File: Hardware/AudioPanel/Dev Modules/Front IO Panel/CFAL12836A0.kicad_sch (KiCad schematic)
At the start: 3 parts, among them U35 CFAL12836A0-088

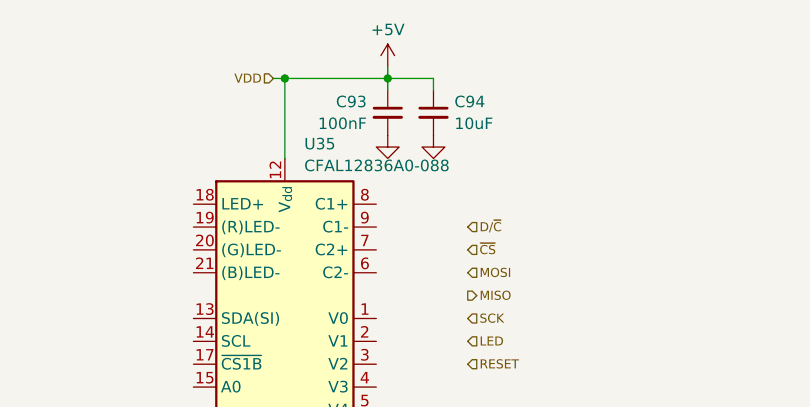
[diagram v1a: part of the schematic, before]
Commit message: Added level shifters for all SAMD21s
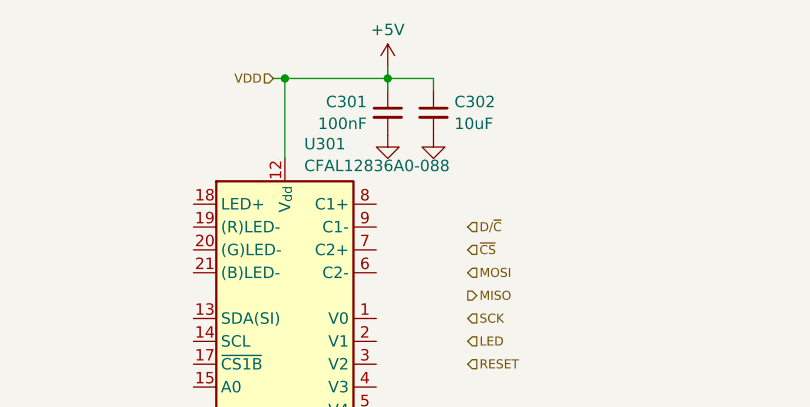
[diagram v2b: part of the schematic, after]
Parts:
- renumbered C93 to C301, C94 to C302, U35 to U301
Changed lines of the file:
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@@
 		(dnp no)
 		(fields_autoplaced yes)
-		(property "Reference" "#PWR?"
+		(property "Reference" "#PWR0301"
 			(at 212.09 86.36 0)
 			(effects
@@
 			(project "Front IO Panel"
 				(path "/5115d310-a9f7-4cd2-bb07-2c33745c004f/c4aba118-8bcc-46b5-ab7c-9e20931e6787"
-					(reference "#PWR?")
+					(reference "#PWR0301")
 					(unit 1)
 				)
@@
 		(dnp no)
 		(fields_autoplaced yes)
-		(property "Reference" "#PWR?"
+		(property "Reference" "#PWR0302"
 			(at 212.09 96.52 0)
 			(effects
@@
 			(project "Front IO Panel"
 				(path "/5115d310-a9f7-4cd2-bb07-2c33745c004f/c4aba118-8bcc-46b5-ab7c-9e20931e6787"
-					(reference "#PWR?")
+					(reference "#PWR0302")
 					(unit 1)
 				)
@@
 		(dnp no)
 		(fields_autoplaced yes)
-		(property "Reference" "U?"
+		(property "Reference" "U301"
 			(at 202.8033 91.1055 0)
 			(effects
@@
 			(project "Front IO Panel"
 				(path "/5115d310-a9f7-4cd2-bb07-2c33745c004f/c4aba118-8bcc-46b5-ab7c-9e20931e6787"
-					(reference "U?")
+					(reference "U301")
 					(unit 1)
 				)
@@
 		(on_board yes)
 		(dnp no)
-		(property "Reference" "C?"
+		(property "Reference" "C302"
 			(at 219.4941 86.4241 0)
 			(effects
@@
 			(project "Front IO Panel"
 				(path "/5115d310-a9f7-4cd2-bb07-2c33745c004f/c4aba118-8bcc-46b5-ab7c-9e20931e6787"
-					(reference "C?")
+					(reference "C302")
 					(unit 1)
 				)
@@
 		(on_board yes)
 		(dnp no)
-		(property "Reference" "C?"
+		(property "Reference" "C301"
 			(at 209.7659 86.4241 0)
 			(effects
@@
 			(project "Front IO Panel"
 				(path "/5115d310-a9f7-4cd2-bb07-2c33745c004f/c4aba118-8bcc-46b5-ab7c-9e20931e6787"
-					(reference "C?")
+					(reference "C301")
 					(unit 1)
 				)
@@
 		(dnp no)
 		(fields_autoplaced yes)
-		(property "Reference" "#PWR?"
+		(property "Reference" "#PWR0303"
 			(at 217.17 96.52 0)
 			(effects
@@
 			(project "Front IO Panel"
 				(path "/5115d310-a9f7-4cd2-bb07-2c33745c004f/c4aba118-8bcc-46b5-ab7c-9e20931e6787"
-					(reference "#PWR?")
-					(unit 1)
-				)
+					(reference "#PWR0303")
+					(unit 1)
+				)

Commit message: Work on front control panel
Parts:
- removed U301: CFAL12836A0-088, Display:NHD-C12832A1Z-FSRGB, symbol Display_Graphic:NHD-C12832A1Z-FSRGB
- added C303: 1u, symbol Device:C_Small
- added C304: 100u, symbol Device:C_Small_US
- added C305: 47u, symbol Device:C_Small
- added C306: 10u, symbol Device:C_Small
- added C307, C308, C309, C310, C314: 100n, symbol Device:C_Small
- added C311: 22u, symbol Device:C_Small
- added C312, C313: 4u7, symbol Device:C_Small
- added D201: Red, LED_THT:LED_D5.0mm, symbol Device:LED_Filled
- added D301: B5817WS-TP, Diode_SMD:D_SOD-323, symbol Device:D_Schottky
- added D302, D303: 1N4148X-TP, Diode_SMD:D_SOD-523, symbol Device:D
- added JP301, JP302: Jumper_2_Small_Open, Jumper:SolderJumper-2_P1.3mm_Open_Pad1.0x1.5mm, symbol Jumper:Jumper_2_Small_Open
- added L301: 10uH, 750mA, symbol Device:L
- added R201: 3k3, Libraries:Worthington_R_0603, symbol Device:R_Small_US
- added R301: 51k, symbol Device:R_Small_US
- added R302: 4k99, symbol Device:R_Small_US
- added R303: 16, symbol Device:R_Small_US
- added R304: 10k, symbol Device:R_Small_US
- added R305: 4k7, symbol Device:R_Small_US
- added TP115: TestPoint_Flag, Libraries:KEYSTONE_5017, symbol Connector:TestPoint_Flag
- added U301: CFAL12836A0, Libraries:CFAL12836A0-088, symbol Libraries:CFAL12836A0
- added U302: AP3012, Package_TO_SOT_SMD:SOT-23-5, symbol Regulator_Switching:AP3012
- C301: value 100nF -> 100n
- C302: value 10uF -> 100n
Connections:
- net GND: now also C303.2, C304.2, C305.2, C306.2, C307.2, C308.2, C309.2, C310.2, C311.2, C312.2, C313.2, C314.2, D302.1 (K), JP302.1 (A), R201.1, R302.2, R305.2, U301.1 (VSS), U301.10 (~{WR}), U301.11 (~{RD}), U301.16 (D2), U301.17 (D3), U301.18 (D4), U301.19 (D5), U301.20 (D6), U301.21 (D7), U301.22 (P/~{S}), U301.27 (VSS), U301.33 (VSS), U301.7 (VSS), U302.2 (GND)
- net MOSI: now also U301.15 (D1(SDIN))
- net SCK: now also U301.14 (D0(SCLK))
- net ~{CS}: now also U301.12 (~{CS})
- net +5V renamed +3V3
- net +3V3: now also C306.1, C309.1, C310.1, C311.1, JP301.1 (A), L301.1, U301.23 (VDDIO), U301.28 (VDD), U301.5 (VDD), U301.8 (VDDIO), U302.5 (IN)
- new net: C303.1, D301.1 (K), R301.1, R303.1
- new net: D301.2 (A), L301.2, U302.1 (SW)
- new net: C314.1, TP115.1, U301.29 (VDDL)
- new net: C312.1, C313.1, R304.1, U301.30 (VCC-R), U301.4 (VCC-R)
- new net: JP302.2 (B), R304.2, U301.6 (PSEL)
- new net: JP301.2 (B), R305.1, U302.4 (~{SHDN})
- new net: R301.2, R302.1, U302.3 (FB)
- new net: D302.2 (A), D303.1 (K)
- new net: D201.1 (K), R201.2
- new net +14V: C304.1, C305.1, C307.1, C308.1, D201.2 (A), R303.2, U301.2 (VCC-C), U301.32 (VCC-C)
- new net A0: U301.13 (A0)
- new net PRE: D303.2 (A), U301.3 (PRE), U301.31 (PRE)
- new net ~{RESET}: U301.9 (~{RST})
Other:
- note added: "3.3V to 14V Boost Supply"
- note added: "The 16ohm+ 47µF filter reduces the current ripple seen on the +3.3v supply line for certain images displayed . The power supply in the Seeeduino v4.2 produces audible noise without this filter. The noise is greatly reduced by the filter. Optionally, you can load the 100µF aluminum electrolytic capacitor which appears to eliminate the audible noise entirely."

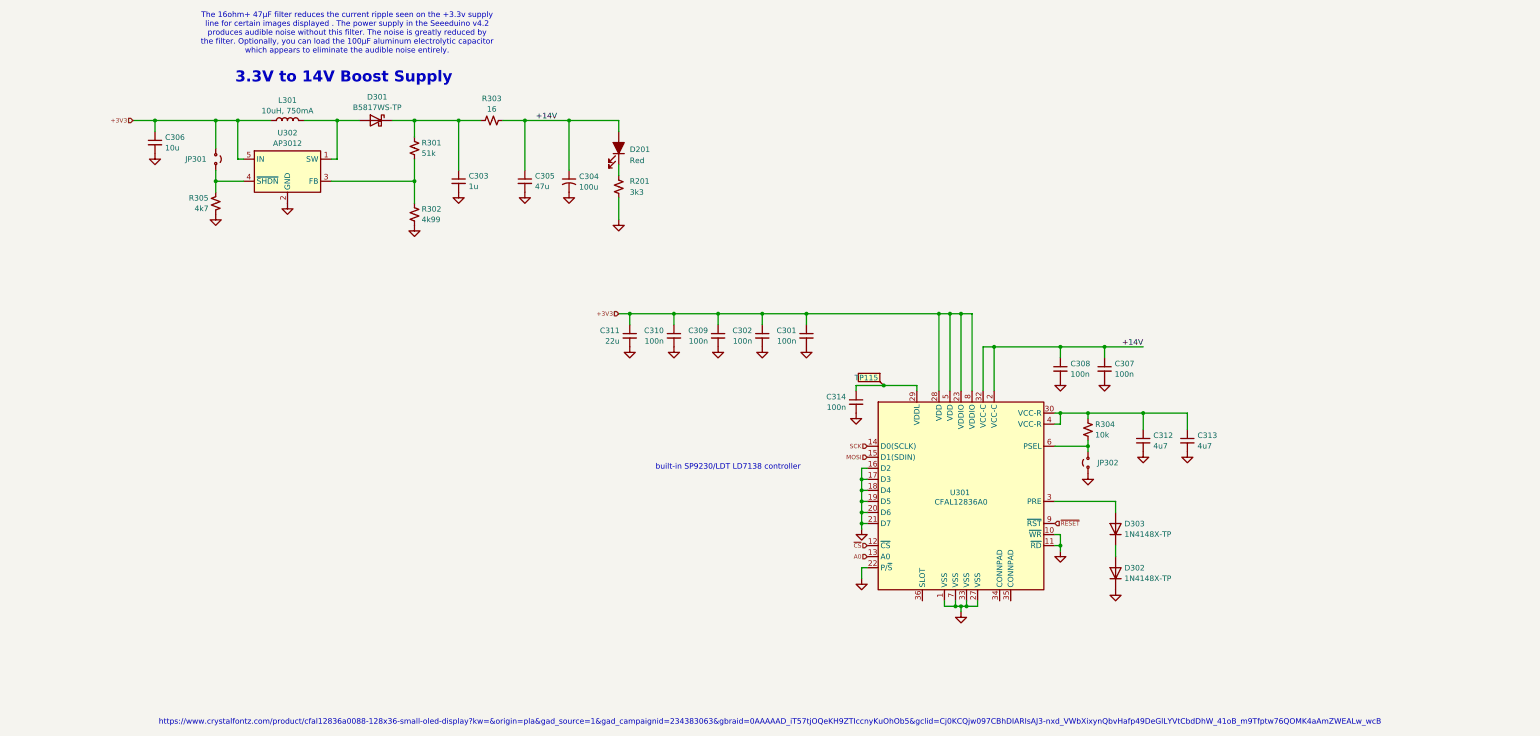
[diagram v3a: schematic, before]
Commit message: Fixed some footprints
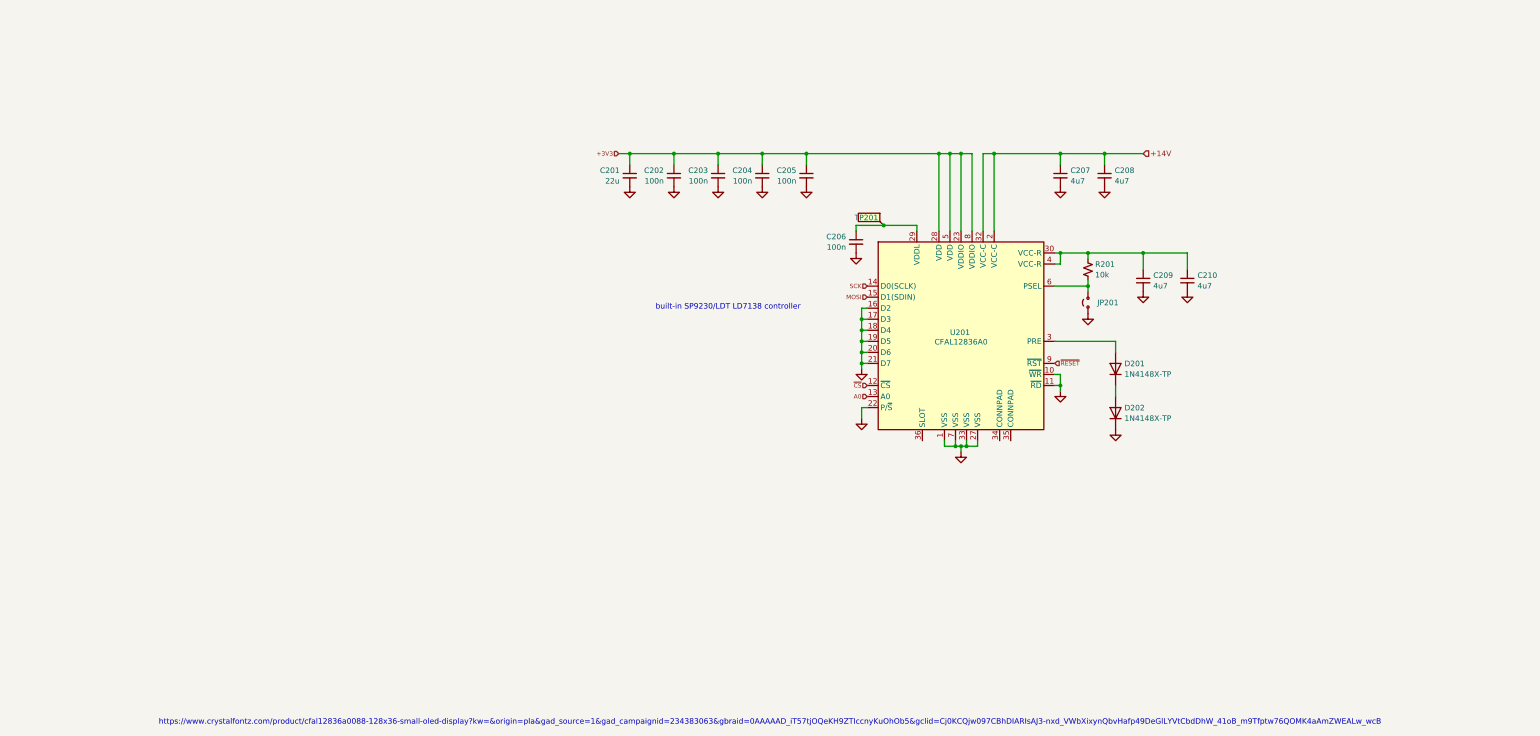
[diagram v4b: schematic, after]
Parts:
- removed C303: 1u, symbol Device:C_Small
- removed C304: 100u, symbol Device:C_Small_US
- removed C305: 47u, symbol Device:C_Small
- removed C306: 10u, symbol Device:C_Small
- removed C307, C308: 100n, symbol Device:C_Small
- removed D201: Red, LED_THT:LED_D5.0mm, symbol Device:LED_Filled
- removed D301: B5817WS-TP, Diode_SMD:D_SOD-323, symbol Device:D_Schottky
- removed JP301: Jumper_2_Small_Open, Jumper:SolderJumper-2_P1.3mm_Open_Pad1.0x1.5mm, symbol Jumper:Jumper_2_Small_Open
- removed L301: 10uH, 750mA, symbol Device:L
- removed R201: 3k3, Libraries:Worthington_R_0603, symbol Device:R_Small_US
- removed R301: 51k, symbol Device:R_Small_US
- removed R302: 4k99, symbol Device:R_Small_US
- removed R303: 16, symbol Device:R_Small_US
- removed R305: 4k7, symbol Device:R_Small_US
- removed U302: AP3012, Package_TO_SOT_SMD:SOT-23-5, symbol Regulator_Switching:AP3012
- added C207, C208: 4u7, Libraries:Worthington_C_0402, symbol Device:C_Small
- C201: renamed from C311; footprint (none) -> Libraries:Worthington_C_0603
- C202: renamed from C310; footprint (none) -> Libraries:Worthington_C_0402
- C203: renamed from C309; footprint (none) -> Libraries:Worthington_C_0402
- C204: renamed from C302; footprint (none) -> Libraries:Worthington_C_0402
- C205: renamed from C301; footprint (none) -> Libraries:Worthington_C_0402
- C206: renamed from C314; footprint (none) -> Libraries:Worthington_C_0402
- C209: renamed from C312; footprint (none) -> Libraries:Worthington_C_0402
- C210: renamed from C313; footprint (none) -> Libraries:Worthington_C_0402
- R201: renamed from R304; footprint (none) -> Libraries:Worthington_R_0402
- renumbered D303 to D201, D302 to D202, JP302 to JP201, TP115 to TP201, U301 to U201
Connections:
- net +14V: now also C207.1, C208.1
- net GND: now also C207.2, C208.2
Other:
- note removed: "3.3V to 14V Boost Supply"
- note removed: "The 16ohm+ 47µF filter reduces the current ripple seen on the +3.3v supply line for certain images displayed . The power supply in the Seeeduino v4.2 produces audible noise without this filter. The noise is greatly reduced by the filter. Optionally, you can load the 100µF aluminum electrolytic capacitor which appears to eliminate the audible noise entirely."
- moved on the sheet: C201, C202, C203, C204, C205, C206, C209, C210, D201, D202, JP201, R201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

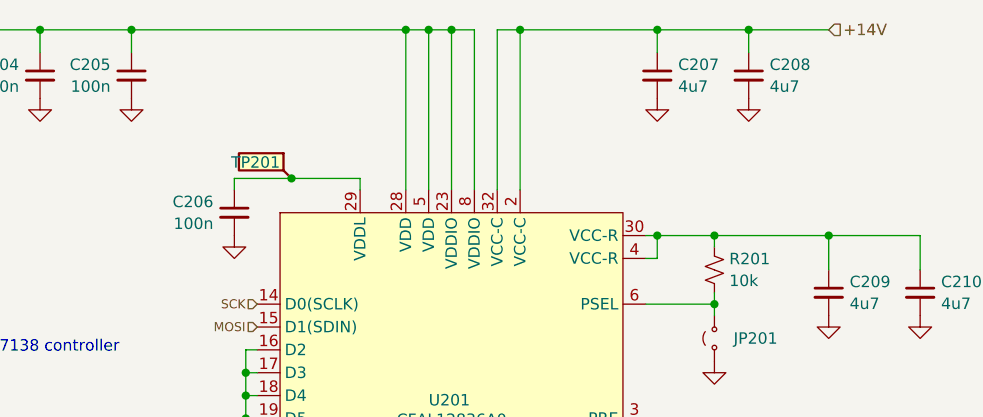
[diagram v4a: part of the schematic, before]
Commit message: Changed encoder, added footprints for buttons
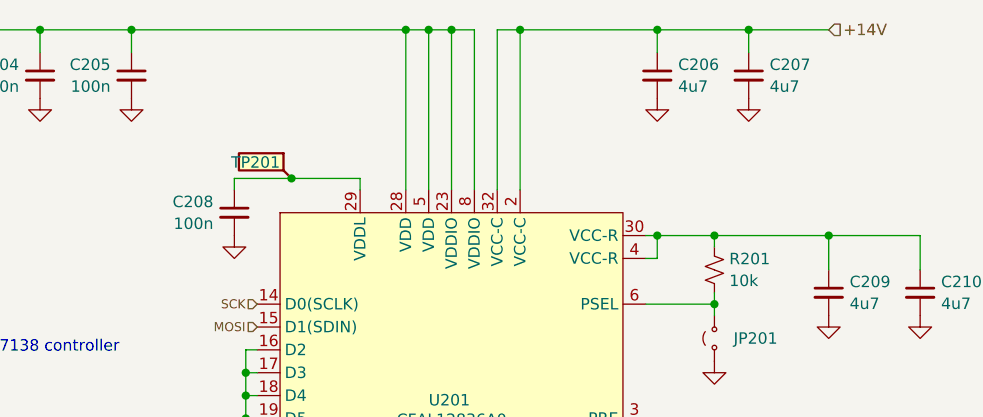
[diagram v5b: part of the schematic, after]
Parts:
- renumbered C207 to C206, C208 to C207, C206 to C208
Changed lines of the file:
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@@
 		(dnp no)
 		(fields_autoplaced yes)
-		(property "Reference" "#PWR0213"
+		(property "Reference" "#PWR0207"
 			(at 248.92 110.49 0)
 			(effects
@@
 			(project "Front IO Panel"
 				(path "/5115d310-a9f7-4cd2-bb07-2c33745c004f/c4aba118-8bcc-46b5-ab7c-9e20931e6787"
-					(reference "#PWR0213")
+					(reference "#PWR0207")
 					(unit 1)
 				)
@@
 		(dnp no)
 		(fields_autoplaced yes)
-		(property "Reference" "#PWR0206"
+		(property "Reference" "#PWR0208"
 			(at 191.77 125.73 0)
 			(effects
@@
 			(project "Front IO Panel"
 				(path "/5115d310-a9f7-4cd2-bb07-2c33745c004f/c4aba118-8bcc-46b5-ab7c-9e20931e6787"
-					(reference "#PWR0206")
+					(reference "#PWR0208")
 					(unit 1)
 				)
@@
 		(dnp no)
 		(fields_autoplaced yes)
-		(property "Reference" "C207"
+		(property "Reference" "C206"
 			(at 241.0841 100.3941 0)
 			(effects
@@
 			(project "Front IO Panel"
 				(path "/5115d310-a9f7-4cd2-bb07-2c33745c004f/c4aba118-8bcc-46b5-ab7c-9e20931e6787"
-					(reference "C207")
+					(reference "C206")
 					(unit 1)
 				)
@@
 		(dnp no)
 		(fields_autoplaced yes)
-		(property "Reference" "C206"
+		(property "Reference" "C208"
 			(at 189.4459 115.6341 0)
 			(effects
@@
 			(project "Front IO Panel"
 				(path "/5115d310-a9f7-4cd2-bb07-2c33745c004f/c4aba118-8bcc-46b5-ab7c-9e20931e6787"
-					(reference "C206")
+					(reference "C208")
 					(unit 1)
 				)
@@
 		(dnp no)
 		(fields_autoplaced yes)
-		(property "Reference" "#PWR0210"
+		(property "Reference" "#PWR0206"
 			(at 238.76 110.49 0)
 			(effects
@@
 			(project "Front IO Panel"
 				(path "/5115d310-a9f7-4cd2-bb07-2c33745c004f/c4aba118-8bcc-46b5-ab7c-9e20931e6787"
-					(reference "#PWR0210")
+					(reference "#PWR0206")
 					(unit 1)
 				)
@@
 		(dnp no)
 		(fields_autoplaced yes)
-		(property "Reference" "C208"
+		(property "Reference" "C207"
 			(at 251.2441 100.3941 0)
 			(effects
@@
 			(project "Front IO Panel"
 				(path "/5115d310-a9f7-4cd2-bb07-2c33745c004f/c4aba118-8bcc-46b5-ab7c-9e20931e6787"
-					(reference "C208")
+					(reference "C207")
 					(unit 1)
 				)
@@
 		(dnp no)
 		(fields_autoplaced yes)
-		(property "Reference" "#PWR0215"
+		(property "Reference" "#PWR0209"
 			(at 257.81 134.62 0)
 			(effects
@@
 			(project "Front IO Panel"
 				(path "/5115d310-a9f7-4cd2-bb07-2c33745c004f/c4aba118-8bcc-46b5-ab7c-9e20931e6787"
-					(reference "#PWR0215")
+					(reference "#PWR0209")
 					(unit 1)
 				)
@@
 		(dnp no)
 		(fields_autoplaced yes)
-		(property "Reference" "#PWR0214"
+		(property "Reference" "#PWR0215"
 			(at 251.46 166.37 0)
 			(effects
@@
 			(project "Front IO Panel"
 				(path "/5115d310-a9f7-4cd2-bb07-2c33745c004f/c4aba118-8bcc-46b5-ab7c-9e20931e6787"
-					(reference "#PWR0214")
+					(reference "#PWR0215")
 					(unit 1)
 				)
@@
 		(dnp no)
 		(fields_autoplaced yes)
-		(property "Reference" "#PWR0211"
+		(property "Reference" "#PWR0213"
 			(at 238.76 157.48 0)
 			(effects
@@
 			(project "Front IO Panel"
 				(path "/5115d310-a9f7-4cd2-bb07-2c33745c004f/c4aba118-8bcc-46b5-ab7c-9e20931e6787"
-					(reference "#PWR0211")
+					(reference "#PWR0213")
 					(unit 1)
 				)
@@
 		(dnp no)
 		(fields_autoplaced yes)
-		(property "Reference" "#PWR0212"
+		(property "Reference" "#PWR0211"
 			(at 245.11 139.7 0)
 			(effects
@@
 			(project "Front IO Panel"
 				(path "/5115d310-a9f7-4cd2-bb07-2c33745c004f/c4aba118-8bcc-46b5-ab7c-9e20931e6787"
-					(reference "#PWR0212")
+					(reference "#PWR0211")
 					(unit 1)
 				)
@@
 		(dnp no)
 		(fields_autoplaced yes)
-		(property "Reference" "#PWR0209"
+		(property "Reference" "#PWR0216"
 			(at 215.9 171.45 0)
 			(effects
@@
 			(project "Front IO Panel"
 				(path "/5115d310-a9f7-4cd2-bb07-2c33745c004f/c4aba118-8bcc-46b5-ab7c-9e20931e6787"
-					(reference "#PWR0209")
+					(reference "#PWR0216")
 					(unit 1)
 				)
@@
 		(dnp no)
 		(fields_autoplaced yes)
-		(property "Reference" "#PWR0208"
+		(property "Reference" "#PWR0214"
 			(at 193.04 163.83 0)
 			(effects
@@
 			(project "Front IO Panel"
 				(path "/5115d310-a9f7-4cd2-bb07-2c33745c004f/c4aba118-8bcc-46b5-ab7c-9e20931e6787"
-					(reference "#PWR0208")
+					(reference "#PWR0214")
 					(unit 1)
 				)
@@
 		(dnp no)
 		(fields_autoplaced yes)
-		(property "Reference" "#PWR0207"
+		(property "Reference" "#PWR0212"
 			(at 193.04 152.4 0)
 			(effects
@@
 			(project "Front IO Panel"
 				(path "/5115d310-a9f7-4cd2-bb07-2c33745c004f/c4aba118-8bcc-46b5-ab7c-9e20931e6787"
-					(reference "#PWR0207")
+					(reference "#PWR0212")
 					(unit 1)
 				)
@@
 		(dnp no)
 		(fields_autoplaced yes)
-		(property "Reference" "#PWR0216"
+		(property "Reference" "#PWR0210"
 			(at 267.97 134.62 0)
 			(effects
@@
 			(project "Front IO Panel"
 				(path "/5115d310-a9f7-4cd2-bb07-2c33745c004f/c4aba118-8bcc-46b5-ab7c-9e20931e6787"
-					(reference "#PWR0216")
-					(unit 1)
-				)
+					(reference "#PWR0210")
+					(unit 1)
+				)
